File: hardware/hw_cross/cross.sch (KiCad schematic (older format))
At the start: 2 parts, among them J1 MOD_IN, J2 MOD_OUT

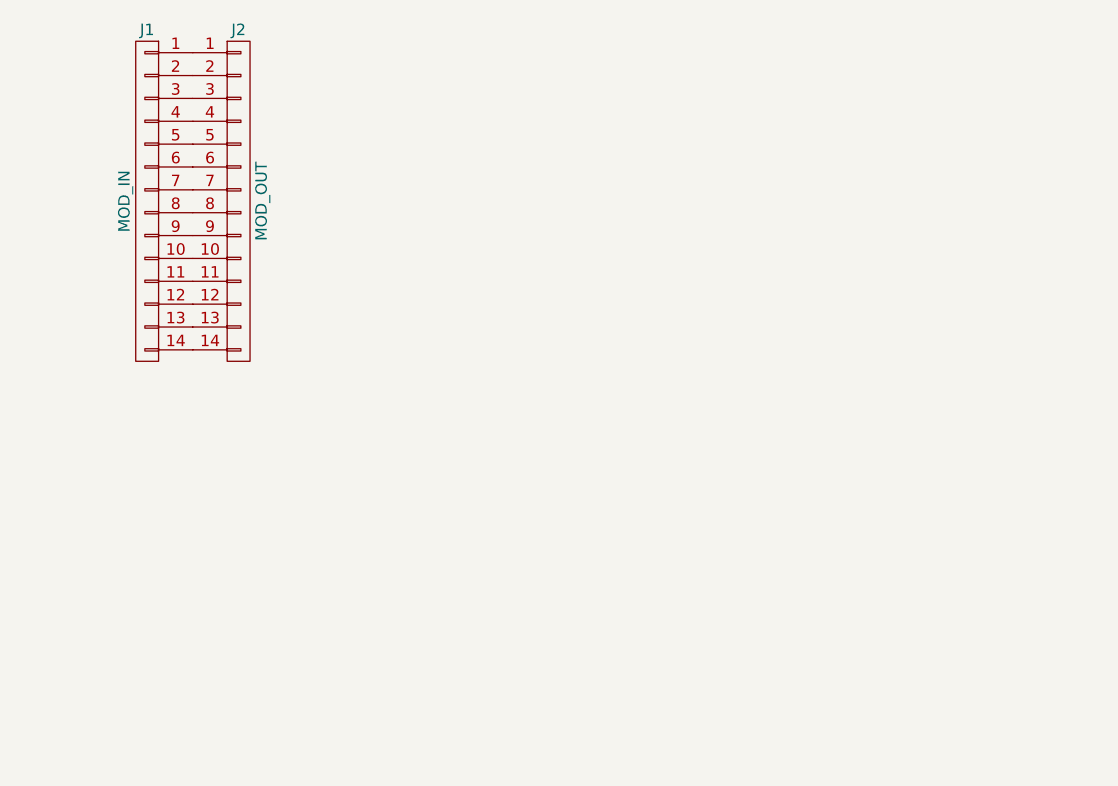
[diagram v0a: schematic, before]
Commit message: Обновлена плата кросс-модуля.
Добавлена буферизация шины.
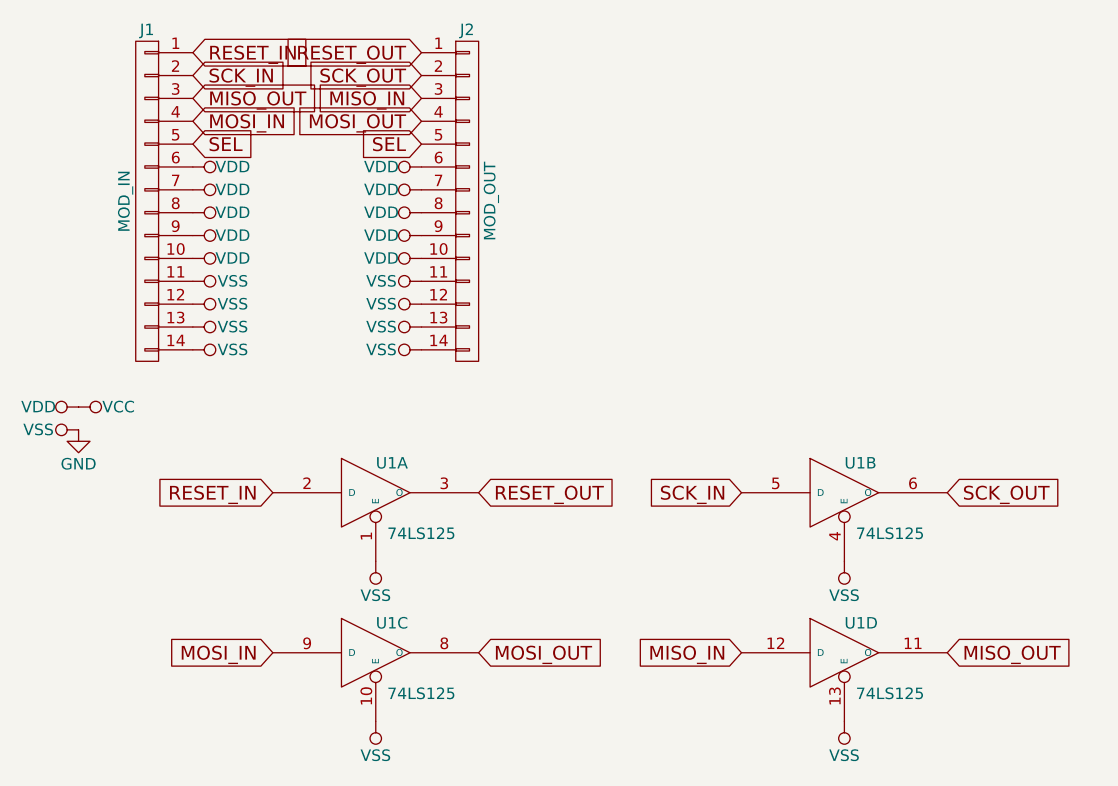
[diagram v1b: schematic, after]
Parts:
- added U1: 74LS125, Housings_SOIC:SOIC-14_3.9x8.7mm_Pitch1.27mm, symbol 74LS125
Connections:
- net RESET_IN: now reaches J1.1 (P1)
- net RESET_IN: now also U1.2 (D); no longer J2.1 (P1)
- net VCC: now reaches J1.10 (P10), J2.10 (P10)
- net VCC: now also J1.6 (P6), J1.7 (P7), J1.8 (P8), J1.9 (P9), J2.6 (P6), J2.7 (P7), J2.8 (P8), J2.9 (P9), U1.14 (VCC), U1.14 (VCC), U1.14 (VCC), U1.14 (VCC)
- net GND: now reaches J1.11 (P11), J2.11 (P11)
- net GND: now also J1.12 (P12), J1.13 (P13), J1.14 (P14), J2.12 (P12), J2.13 (P13), J2.14 (P14), U1.1 (E), U1.10 (E), U1.13 (E), U1.4 (E), U1.7 (GND), U1.7 (GND), U1.7 (GND), U1.7 (GND)
- net SCK_IN: now reaches J1.2 (P2)
- net SCK_IN: now also U1.5 (D); no longer J2.2 (P2)
- net MISO_IN: now reaches J2.3 (P3)
- net MISO_IN: now also U1.12 (D); no longer J1.3 (P3)
- net MOSI_IN: now reaches J1.4 (P4)
- net MOSI_IN: now also U1.9 (D); no longer J2.4 (P4)
- net SEL: now reaches J1.5 (P5), J2.5 (P5)
- new net MISO_OUT: J1.3 (P3), U1.11 (O)
- new net MOSI_OUT: J2.4 (P4), U1.8 (O)
- new net RESET_OUT: J2.1 (P1), U1.3 (O)
- new net SCK_OUT: J2.2 (P2), U1.6 (O)
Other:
- moved on the sheet: J2
